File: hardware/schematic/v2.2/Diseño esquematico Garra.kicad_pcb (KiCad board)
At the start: 2 copper layers, 85.5 x 136.7 mm, 29 parts

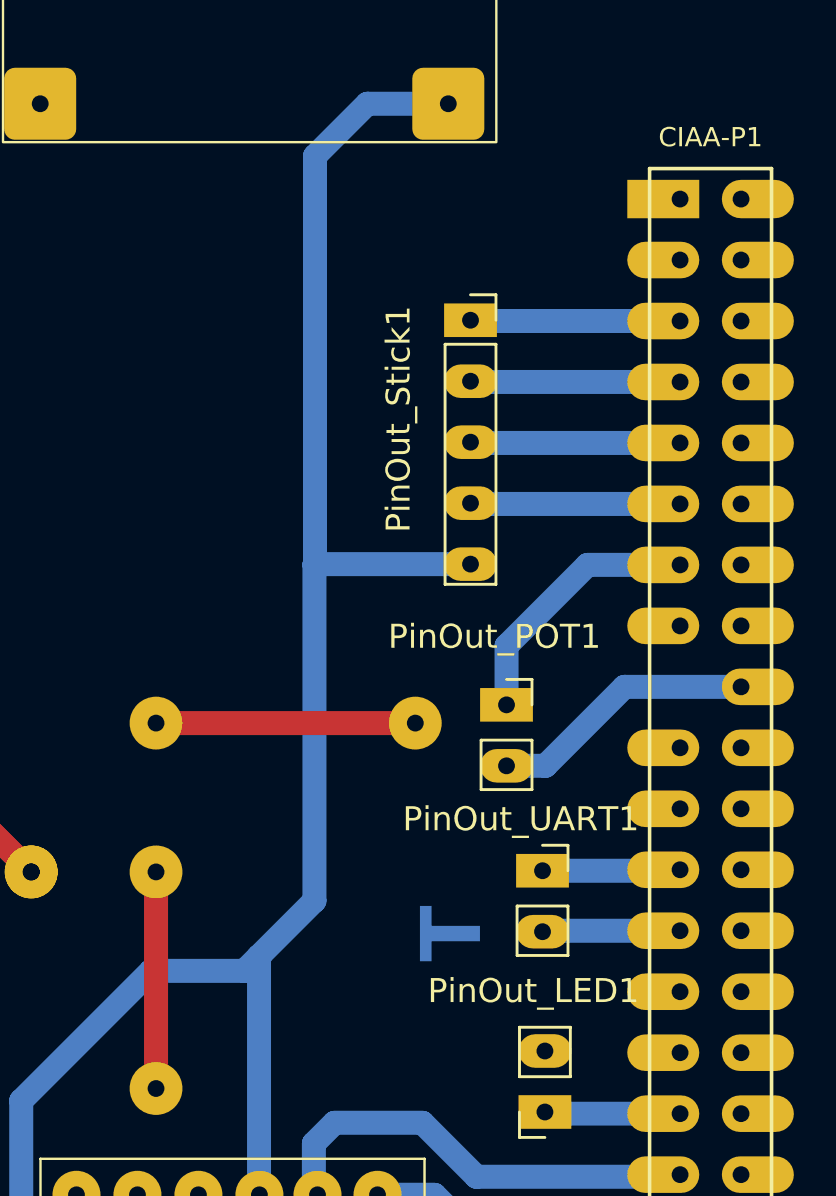
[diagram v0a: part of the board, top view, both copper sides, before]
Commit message: feat: Change Stick_on from ISP to CAN_RD
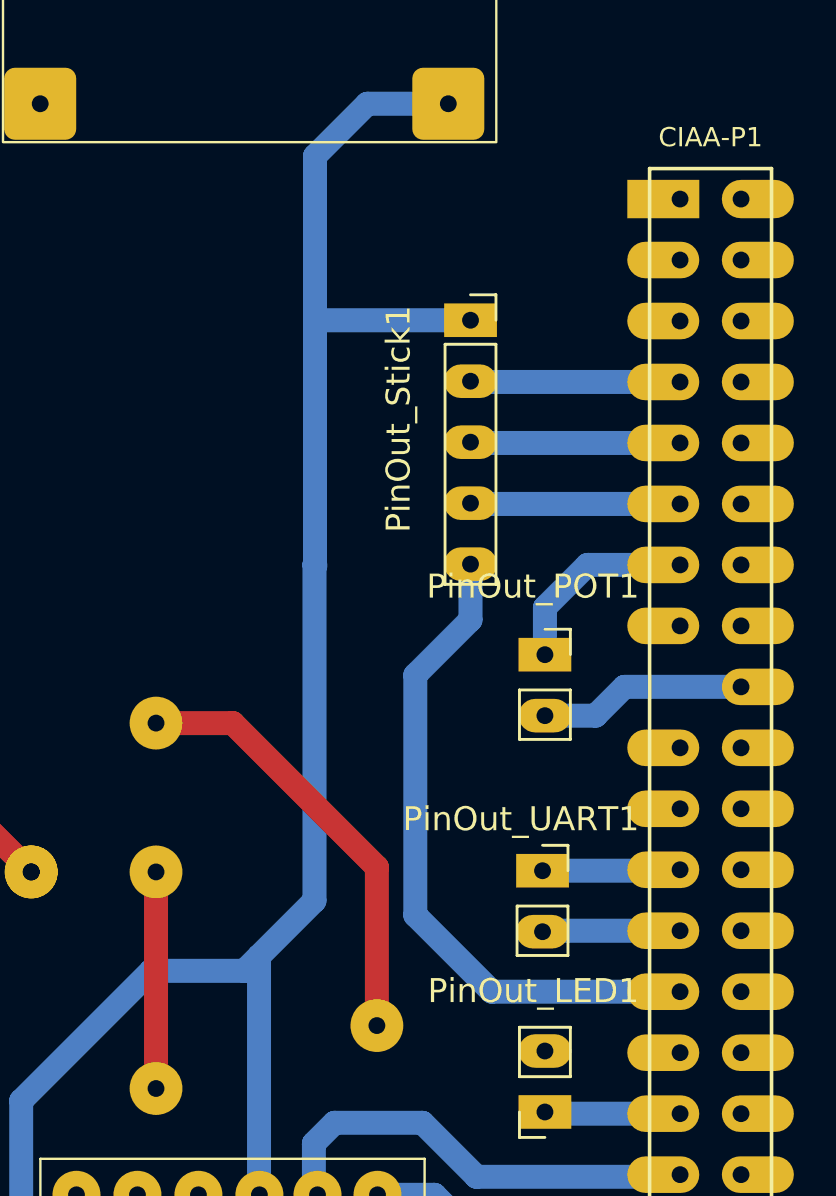
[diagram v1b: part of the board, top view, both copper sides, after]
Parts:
- moved ? 12.7 mm to (99.6, 122.2)
- moved PinOut_POT1 2.63 mm to (106.6, 106.8)
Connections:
- CIAA-P1 pad 27: unconnected-(CIAA-P1-CAN_RD-Pad27) -> Stick_ON
- CIAA-P1 pad 5: Stick_ON -> unconnected-(CIAA-P1-ISP-Pad5)
- PinOut_Stick1 pad 1: Stick_ON -> 5V
- PinOut_Stick1 pad 5: 5V -> Stick_ON
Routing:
- net Stick_ON: track 8.74 -> 28.1 mm
- net GND: track 56.2 -> 63.7 mm
- net POT: track 11.1 -> 8.38 mm
- net GND_POT: track 11.1 -> 8.67 mm
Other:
- board text removed: "T"
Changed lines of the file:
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@@
 	(net 61 "unconnected-(CIAA-P1-TFIL1-Pad36)")
 	(net 62 "unconnected-(CIAA-P1-CAN_TD-Pad29)")
-	(net 63 "unconnected-(CIAA-P1-CAN_RD-Pad27)")
+	(net 63 "unconnected-(CIAA-P1-ISP-Pad5)")
 	(net 64 "unconnected-(CIAA-P1-I2C_SCL-Pad21)")
 	(net 65 "unconnected-(CIAA-P1-TCOL0-Pad39)")
@@
 	(footprint ""
 		(layer "F.Cu")
-		(at 101.2 109.6)
+		(at 99.6 122.2)
 		(property "Reference" ""
 			(at 0 0 0)
@@
 			(layers "*.Cu" "*.Mask")
 			(remove_unused_layers no)
-			(net 81 "Stick_ON")
+			(net 11 "5V")
 			(pinfunction "Pin_1")
 			(pintype "passive")
@@
 			(layers "*.Cu" "*.Mask")
 			(remove_unused_layers no)
-			(net 11 "5V")
+			(net 81 "Stick_ON")
 			(pinfunction "Pin_5")
 			(pintype "passive")
@@
 			(layers "*.Cu" "*.Mask" "F.SilkS")
 			(remove_unused_layers no)
-			(net 81 "Stick_ON")
+			(net 63 "unconnected-(CIAA-P1-ISP-Pad5)")
 			(pinfunction "ISP")
 			(pintype "passive")
@@
 			(layers "*.Cu" "*.Mask" "F.SilkS")
 			(remove_unused_layers no)
-			(net 63 "unconnected-(CIAA-P1-CAN_RD-Pad27)")
+			(net 81 "Stick_ON")
 			(pinfunction "CAN_RD")
 			(pintype "passive")
@@
 	(footprint "LIBRERIA_EDU_CIAA_NXP:PinSocket_1x02_P2.54mm_Vertical"
 		(layer "F.Cu")
-		(at 105 108.84)
+		(at 106.6 106.75)
 		(descr "Through hole straight socket strip, 1x02, 2.00mm pitch, single row (from Kicad 4.0.7), script generated")
 		(tags "Through hole socket strip THT 1x02 2.00mm single row")
@@
 		)
 	)
-	(gr_text "T\n"
-		(at 104.2 117.2 90)
-		(layer "B.Cu")
-		(effects
-			(font
-				(size 2.5 2.5)
-				(thickness 0.5)
-				(bold yes)
-			)
-			(justify left bottom mirror)
-		)
-	)
 	(segment
 		(start 89.52 144.776)
@@
 	)
 	(segment
+		(start 97.04 92.818)
+		(end 97.022 92.8)
+		(width 1)
+		(layer "B.Cu")
+		(net 11)
+	)
+	(segment
 		(start 106 155.25)
 		(end 106 146.5)
@@
 	)
 	(segment
+		(start 97.022 85.978)
+		(end 97.022 92.8)
+		(width 1)
+		(layer "B.Cu")
+		(net 11)
+	)
+	(segment
 		(start 97 117)
 		(end 97 103)
@@
 	)
 	(segment
+		(start 103.532 92.85)
+		(end 103.5 92.818)
+		(width 1)
+		(layer "B.Cu")
+		(net 11)
+	)
+	(segment
 		(start 102.575 83.8)
 		(end 99.2 83.8)
@@
 	)
 	(segment
-		(start 103.5 102.978)
-		(end 97.022 102.978)
-		(width 1)
-		(layer "B.Cu")
-		(net 11)
-	)
-	(segment
-		(start 97.022 85.978)
+		(start 97.022 92.8)
 		(end 97.022 102.978)
 		(width 1)
@@
 	)
 	(segment
+		(start 103.5 92.818)
+		(end 97.04 92.818)
+		(width 1)
+		(layer "B.Cu")
+		(net 11)
+	)
+	(segment
 		(start 78.18 92.31)
 		(end 79.45 93.58)
@@
 	)
 	(segment
+		(start 93.6 109.6)
+		(end 90.4 109.6)
+		(width 1)
+		(layer "F.Cu")
+		(net 13)
+	)
+	(segment
 		(start 90.4 124.822)
 		(end 90.4 115.8)
@@
 	)
 	(segment
-		(start 53.8 103.4)
-		(end 50.4 100)
+		(start 99.6 115.6)
+		(end 93.6 109.6)
 		(width 1)
 		(layer "F.Cu")
@@
 	)
 	(segment
-		(start 101.2 109.6)
-		(end 90.4 109.6)
+		(start 53.8 103.4)
+		(end 50.4 100)
 		(width 1)
 		(layer "F.Cu")
@@
 	)
 	(segment
-		(start 109.91 108.09)
-		(end 106.62 111.38)
+		(start 99.6 122.2)
+		(end 99.6 115.6)
+		(width 1)
+		(layer "F.Cu")
+		(net 13)
+	)
+	(segment
+		(start 108.71 109.29)
+		(end 106.6 109.29)
 		(width 1)
 		(layer "B.Cu")
@@
 	)
 	(segment
-		(start 106.62 111.38)
-		(end 105 111.38)
+		(start 109.91 108.09)
+		(end 108.71 109.29)
 		(width 1)
 		(layer "B.Cu")
@@
 	)
 	(segment
-		(start 105 108.84)
-		(end 105 106.384)
+		(start 106.6 104.784)
+		(end 108.374 103.01)
 		(width 1)
 		(layer "B.Cu")
@@
 	)
 	(segment
-		(start 105 106.384)
-		(end 108.374 103.01)
+		(start 112.198 102.978)
+		(end 112.23 103.01)
 		(width 1)
 		(layer "B.Cu")
@@
 	)
 	(segment
-		(start 108.374 103.01)
-		(end 112.23 103.01)
+		(start 106.6 106.75)
+		(end 106.6 104.784)
 		(width 1)
 		(layer "B.Cu")
@@
 	)
 	(segment
-		(start 112.198 102.978)
+		(start 108.374 103.01)
 		(end 112.23 103.01)
 		(width 1)
@@
 	)
 	(segment
-		(start 103.532 92.85)
-		(end 103.5 92.818)
+		(start 103.4 103.078)
+		(end 103.5 102.978)
+		(width 1)
+		(layer "B.Cu")
+		(net 81)
+	)
+	(segment
+		(start 103.5 105.3)
+		(end 101.2 107.6)
+		(width 1)
+		(layer "B.Cu")
+		(net 81)
+	)
+	(segment
+		(start 101.2 107.6)
+		(end 101.2 117.6)
+		(width 1)
+		(layer "B.Cu")
+		(net 81)
+	)
+	(segment
+		(start 101.2 117.6)
+		(end 104.39 120.79)
 		(width 1)
 		(layer "B.Cu")
@@
 	)
 	(segment
-		(start 112.23 92.85)
-		(end 103.532 92.85)
+		(start 104.39 120.79)
+		(end 112.23 120.79)
+		(width 1)
+		(layer "B.Cu")
+		(net 81)
+	)
+	(segment
+		(start 103.5 102.978)
+		(end 103.5 105.3)
 		(width 1)
 		(layer "B.Cu")
